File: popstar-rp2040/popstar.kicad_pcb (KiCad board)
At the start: 2 copper layers, 284.7 x 94.2 mm, 182 parts, among them J1 JST SH 4-pin, J2 SWD, SW1 Boot, SW10 MX_SW_solder, SW11 MX_SW_solder, SW12 MX_SW_solder, SW13 MX_SW_solder, SW14 MX_SW_solder, SW15 MX_SW_solder, SW16 MX_SW_solder, SW17 MX_SW_solder, SW18 MX_SW_solder, SW19 MX_SW_solder, SW2 MX_SW_solder, SW20 MX_SW_solder, SW21 MX_SW_solder, SW22 MX_SW_solder, SW23 MX_SW_solder, SW24 MX_SW_solder, SW25 MX_SW_solder, SW26 MX_SW_solder, SW27 MX_SW_solder, SW28 MX_SW_solder, SW29 MX_SW_solder, SW3 MX_SW_solder, SW30 MX_SW_solder, SW31 MX_SW_solder, SW32 MX_SW_solder, SW33 MX_SW_solder, SW34 MX_SW_solder, SW35 MX_SW_solder, SW36 MX_SW_solder, SW37 MX_SW_solder, SW38 MX_SW_solder, SW39 MX_SW_solder, SW4 MX_SW_solder, SW40 MX_SW_solder, SW41 MX_SW_solder, SW42 MX_SW_solder, SW43 MX_SW_solder, SW44 MX_SW_solder, SW45 MX_SW_solder, SW46 MX_SW_solder, SW47 MX_SW_solder, SW48 MX_SW_solder, SW49 MX_SW_solder, SW5 MX_SW_solder, SW50 MX_SW_solder, SW51 MX_SW_solder, SW52 MX_SW_solder, SW53 MX_SW_solder, SW54 MX_SW_solder, SW55 MX_SW_solder, SW56 MX_SW_solder, SW57 MX_SW_solder, SW58 MX_SW_solder, SW59 MX_SW_solder, SW6 MX_SW_solder, SW60 MX_SW_solder, SW61 MX_SW_solder, SW62 MX_SW_solder, SW7 MX_SW_solder, SW8 MX_SW_solder, SW9 MX_SW_solder, U2 XC6206PxxxMR, U3 SRV05-4, U4 W25Q128JVS, U5 74AHCT1G125, U6 RP2040, Y1 12MHz

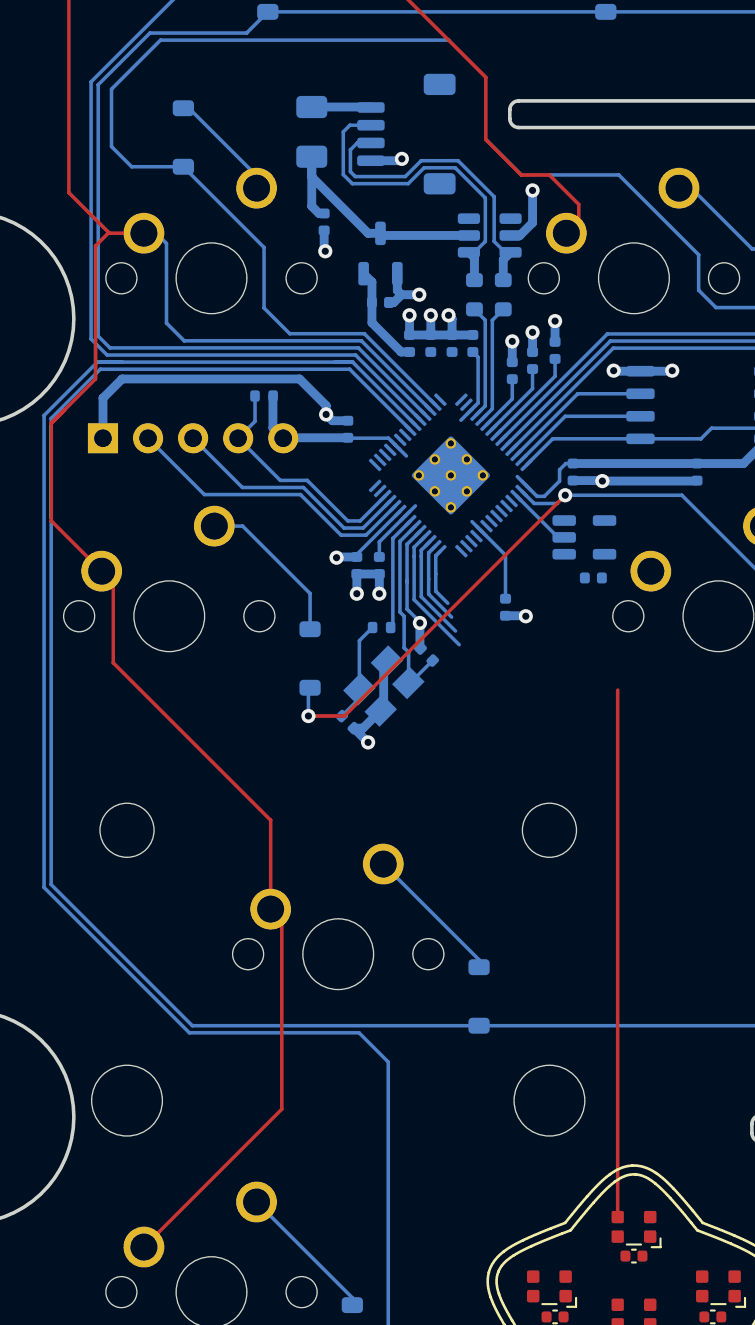
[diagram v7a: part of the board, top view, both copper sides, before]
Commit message: Updated traces near voltage step up component
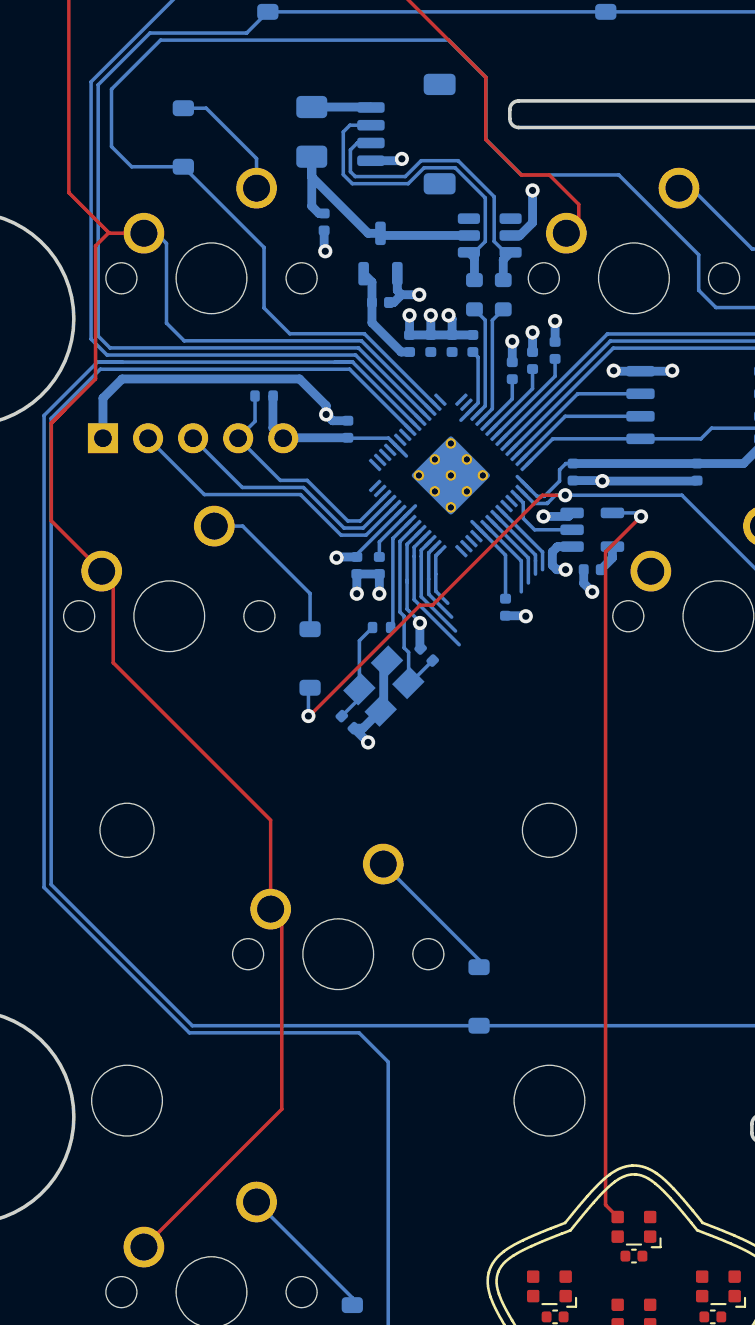
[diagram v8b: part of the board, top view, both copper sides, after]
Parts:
- moved U5 0.62 mm to (67.5, 74.5)
- moved C18 0.47 mm to (67.5, 76.8)
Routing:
- net ARGB_5V: track 29.7 -> 42.3 mm, vias 0 -> 1
- net GND: track 68.5 -> 74.5 mm, vias 20 -> 23
- net COL05: track 0.00 -> 4.52 mm
- net COL04: track 0.00 -> 4.35 mm
- net COL02: track 0.00 -> 4.26 mm
- net COL03: track 0.00 -> 4.18 mm
- net +5V: track 15.0 -> 16.6 mm
- net ARGB_3V3: track 3.65 -> 4.44 mm
- net COL00: track 113.3 -> 112.6 mm
